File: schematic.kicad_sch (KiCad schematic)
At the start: 6 parts, among them J3 USB_C_Receptacle_USB2.0_16P

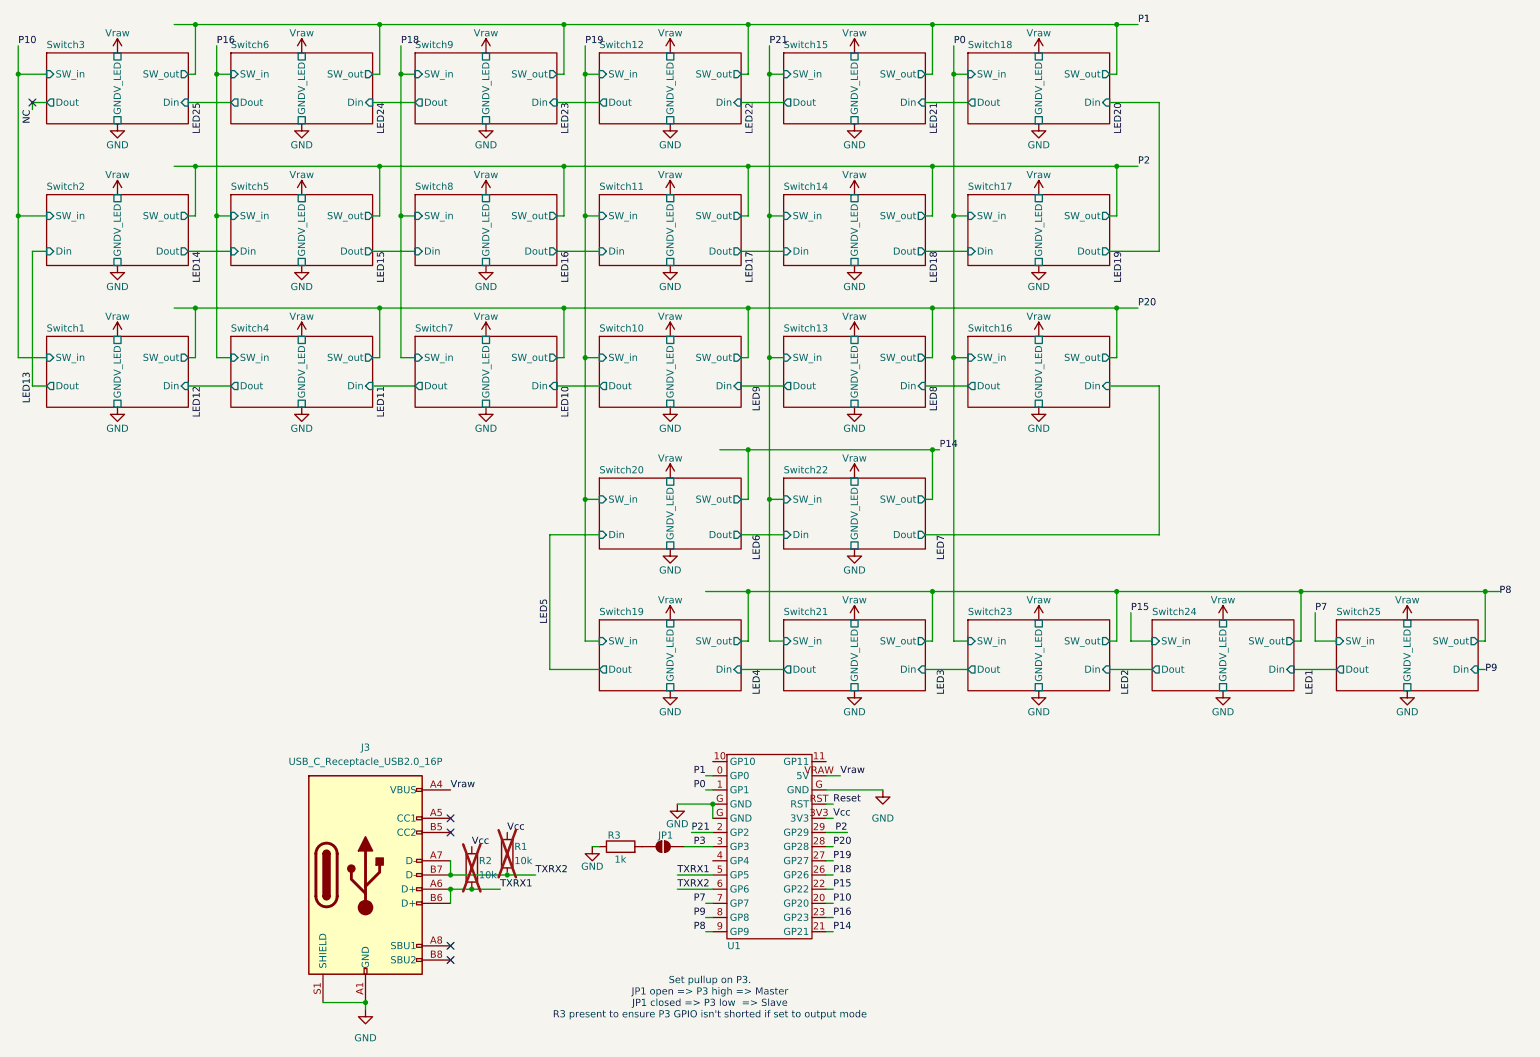
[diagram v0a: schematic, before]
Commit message: Add mounting holes and TVS diodes
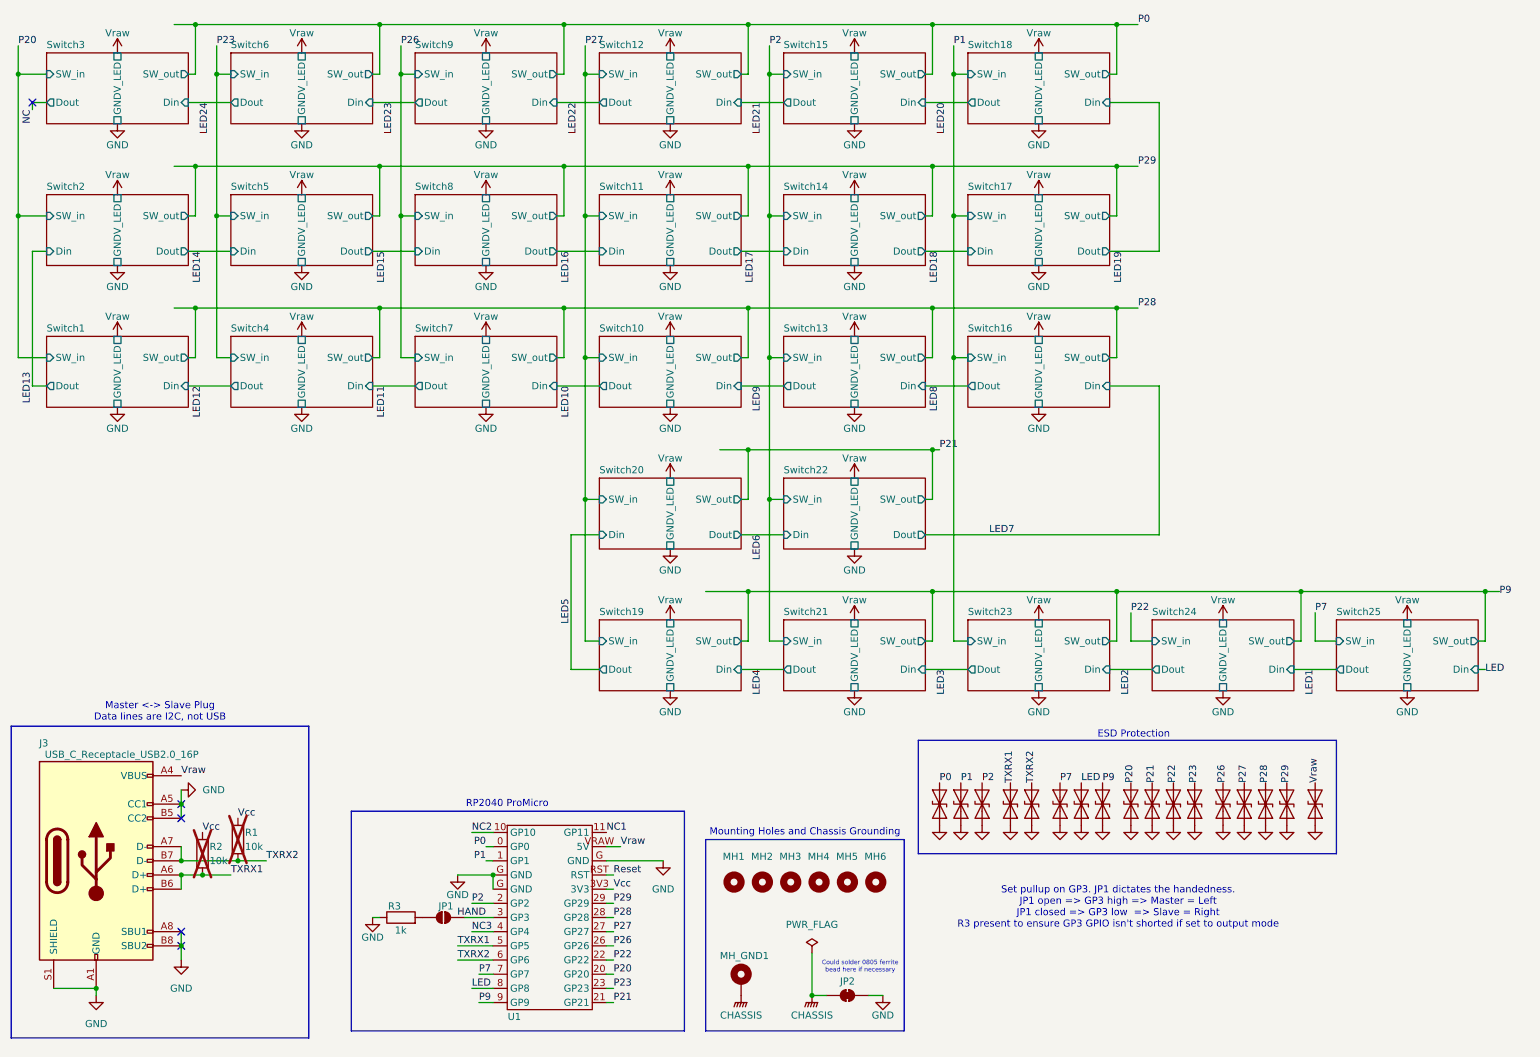
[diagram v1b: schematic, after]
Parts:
- added D26, D27, D28, D29, D30, D31, D32, D33, D34, D35, D36, D37, D38, D39, D40, D41, D42: ESD5Z5.0C, Diode_SMD:D_SOD-523, symbol Diode:ESD9B3.3ST5G
- added JP2: SolderJumper_2_Bridged, Jumper:SolderJumper-2_P1.3mm_Bridged_RoundedPad1.0x1.5mm, symbol Jumper:SolderJumper_2_Bridged
- added MH1, MH2, MH3, MH4, MH5, MH6: MountingHole_Pad, MountingHole:MountingHole_3mm_Pad_Via, symbol Mechanical:MountingHole
- added MH_GND1: MountingHole_Pad, MountingHole:MountingHole_3mm_Pad_Via, symbol Mechanical:MountingHole_Pad
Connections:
- net P10 is gone; now on net P20: U1.20 (GP20)
- net P14 is gone; now on net P21: U1.21 (GP21)
- net P8 is gone; now on net P9: U1.9 (GP9)
- net GND: now also J3.A5 (CC1), J3.A8 (SBU1), J3.B5 (CC2), J3.B8 (SBU2), D26.1 (A1), D27.1 (A1), D28.1 (A1), D29.1 (A1), D30.1 (A1), D31.1 (A1), D32.1 (A1), D33.1 (A1), D34.1 (A1), D35.1 (A1), D36.1 (A1), D37.1 (A1), D38.1 (A1), D39.1 (A1), D40.1 (A1), D41.1 (A1), D42.1 (A1), JP2.2 (B)
- net P0: now also U1.0 (GP0), D26.2 (A2); no longer U1.1 (GP1)
- net P1: now also U1.1 (GP1), D27.2 (A2); no longer U1.0 (GP0)
- net P2: now also U1.2 (GP2), D28.2 (A2); no longer U1.29 (GP29)
- net P20: now also D34.2 (A2); no longer U1.28 (GP28)
- net P21: now also D35.2 (A2); no longer U1.2 (GP2)
- net P7: now also D31.2 (A2)
- net P9: now also D33.2 (A2); no longer U1.8 (GP8)
- net TXRX1: now also D29.2 (A2)
- net TXRX2: now also D30.2 (A2)
- net Vraw: now also D42.2 (A2)
- net NC2: now reaches U1.10 (GP10)
- net NC1: now reaches U1.11 (GP11)
- net NC3: now reaches U1.4 (GP4)
- net P15 renamed P22
- net P22: now also D36.2 (A2)
- net P16 renamed P23
- net P23: now also D37.2 (A2)
- net P18 renamed P26
- net P26: now also D38.2 (A2)
- net P19 renamed P27
- net P27: now also D39.2 (A2)
- net P3 renamed HAND
- new net CHASSIS: JP2.1 (A), MH_GND1.1
- new net LED: D32.2 (A2), U1.8 (GP8)
- new net P28: D40.2 (A2), U1.28 (GP28)
- new net P29: D41.2 (A2), U1.29 (GP29)
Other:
- note added: "Could solder 0805 ferrite bead here if necessary"
- note added: "ESD Protection"
- note added: "Master <-> Slave Plug Data lines are I2C, not USB"
- note added: "Mounting Holes and Chassis Grounding"
- note added: "RP2040 ProMicro"
- note added: "Set pullup on GP3. JP1 dictates the handedness. JP1 open => GP3 high => Master = Left JP1 closed => GP3 low => Slave = Right R3 present to ensure GP3 GPIO isn't shorted if set to output mode"
- note removed: "Set pullup on P3. JP1 open => P3 high => Master JP1 closed => P3 low => Slave R3 present to ensure P3 GPIO isn't shorted if set to output mode"
- moved on the sheet: J3, JP1, R1, R2, R3, U1

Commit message: Replace LEDs with reverse mount variant
Previous LEDs collided with switch
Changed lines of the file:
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@@
-	(wire
-		(pts
-			(xy 17.78 30.48) (xy 17.78 29.21)
-		)
-		(stroke
-			(width 0)
-			(type default)
-			(color 3 116 255 1)
-		)
-	)
 	(wire
 		(pts
@@
 		)
 	)
-	(label "NC"
-		(at 17.78 30.48 270)
-		(fields_autoplaced yes)
-		(effects
-			(font
-				(size 1.27 1.27)
-			)
-			(justify right bottom)
-		)
-	)

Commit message: Add external pullup resistors
Just in case
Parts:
- added R10, R11, R4, R5, R6, R7, R8, R9: 10k, Resistor_SMD:R_0805_2012Metric_Pad1.20x1.40mm_HandSolder, symbol Device:R
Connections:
- net P1: now also R11.2
- net P2: now also R4.2
- net P20: now also R6.2
- net P22: now also R7.2
- net P23: now also R8.2
- net P26: now also R9.2
- net P27: now also R10.2
- net P7: now also R5.2
- net Vcc: now also R10.1, R11.1, R4.1, R5.1, R6.1, R7.1, R8.1, R9.1
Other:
- note added: "External pullups"
- note added: "Master <-> Slave Plug Data lines are UART/I2C, not USB"
- note removed: "Master <-> Slave Plug Data lines are I2C, not USB"
